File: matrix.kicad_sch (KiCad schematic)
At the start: 129 parts

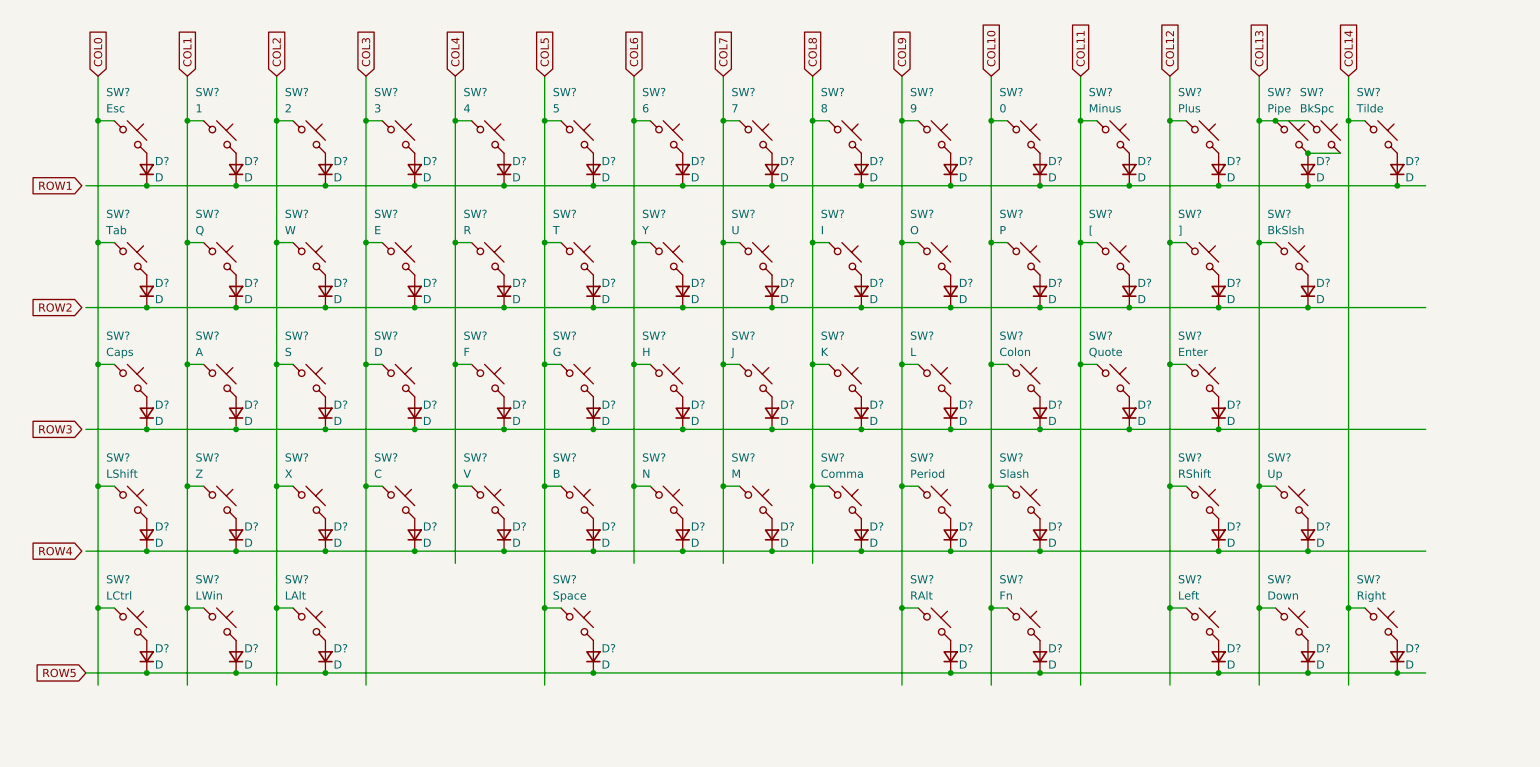
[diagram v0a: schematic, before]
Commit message: did initial routing of MCU and USB
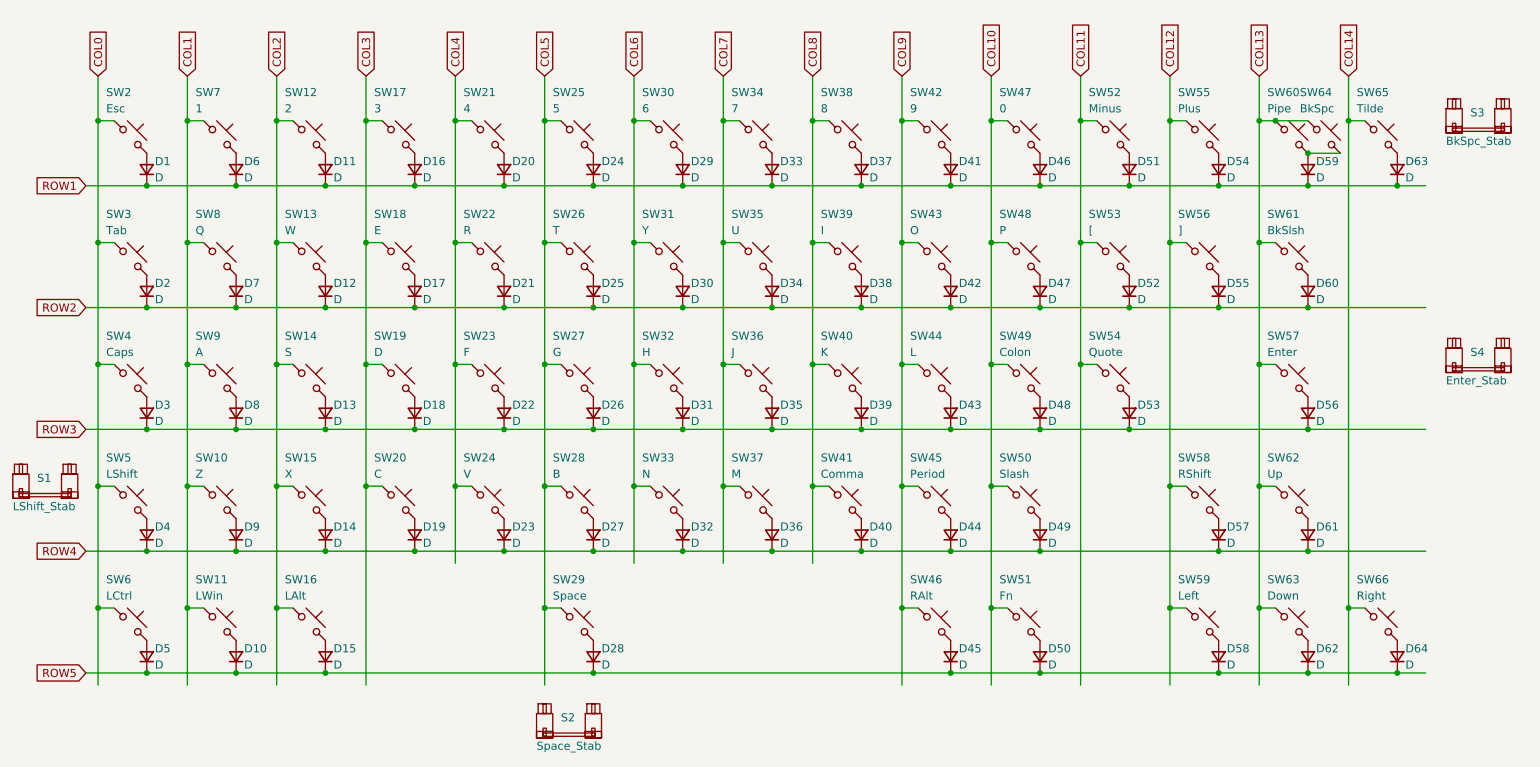
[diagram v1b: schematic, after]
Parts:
- added S1: LShift_Stab, marbastlib-mx:STAB_MX_P_2.25u, symbol marbastlib-mx:MX_stab
- added S2: Space_Stab, marbastlib-mx:STAB_MX_P_6.25u, symbol marbastlib-mx:MX_stab
- added S3: BkSpc_Stab, marbastlib-mx:STAB_MX_P_2u, symbol marbastlib-mx:MX_stab
- added S4: Enter_Stab, marbastlib-mx:STAB_MX_P_2.25u, symbol marbastlib-mx:MX_stab
- D1, D10, D11, D12, D13, D14, D15, D16, D17, D18, D19, D2, D20, D21, D22, D23, D24, D25, D26, D27, D28, D29, D3, D30, D31, D32, D33, D34, D35, D36, D37, D38, D39, D4, D40, D41, D42, D43, D44, D45, D46, D47, D48, D49, D5, D50, D51, D52, D53, D54, D55, D56, D57, D58, D59, D6, D60, D61, D62, D63, D64, D7, D8, D9: renamed from D?; footprint (none) -> Diode_SMD:D_0805_2012Metric_Pad1.15x1.40mm_HandSolder
- SW11, SW16, SW46, SW51, SW6: renamed from SW?; footprint marbastlib-mx:SW_MX_HS_1u -> marbastlib-mx:SW_MX_HS_1.25u
- SW3, SW61: renamed from SW?; footprint marbastlib-mx:SW_MX_HS_1u -> marbastlib-mx:SW_MX_HS_1.5u
- SW4, SW58: renamed from SW?; footprint marbastlib-mx:SW_MX_HS_1u -> marbastlib-mx:SW_MX_HS_1.75u
- gave numbers to parts that had none: 56
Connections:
- net COL12: no longer SW57.1
- net COL13: now also SW57.1
- net ROW1: now also D1.1 (K), D11.1 (K), D16.1 (K), D20.1 (K), D24.1 (K), D29.1 (K), D33.1 (K), D37.1 (K), D41.1 (K), D46.1 (K), D51.1 (K), D54.1 (K), D59.1 (K), D6.1 (K), D63.1 (K)
- net ROW2: now also D12.1 (K), D17.1 (K), D2.1 (K), D21.1 (K), D25.1 (K), D30.1 (K), D34.1 (K), D38.1 (K), D42.1 (K), D47.1 (K), D52.1 (K), D55.1 (K), D60.1 (K), D7.1 (K)
- net ROW3: now also D13.1 (K), D18.1 (K), D22.1 (K), D26.1 (K), D3.1 (K), D31.1 (K), D35.1 (K), D39.1 (K), D43.1 (K), D48.1 (K), D53.1 (K), D56.1 (K), D8.1 (K)
- net ROW4: now also D14.1 (K), D19.1 (K), D23.1 (K), D27.1 (K), D32.1 (K), D36.1 (K), D4.1 (K), D40.1 (K), D44.1 (K), D49.1 (K), D57.1 (K), D61.1 (K), D9.1 (K)
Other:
- moved on the sheet: D56, SW57

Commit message: routed columns
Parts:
- renumbered D57 to D56, D58 to D57, D59 to D58, D60 to D59, D56 to D60, SW9 to SW10, SW10 to SW11, SW11 to SW12, SW12 to SW13, SW13 to SW14, SW14 to SW15, SW15 to SW16, SW16 to SW17, SW17 to SW18, SW18 to SW19, SW19 to SW20, SW20 to SW21, SW21 to SW22, SW22 to SW23, SW23 to SW24, SW24 to SW25, SW25 to SW26, SW26 to SW27, SW27 to SW28, SW28 to SW29, SW2 to SW3, SW29 to SW30, SW30 to SW31, SW31 to SW32, SW32 to SW33, SW33 to SW34, SW34 to SW35, SW35 to SW36, SW36 to SW37, SW37 to SW38, SW38 to SW39, SW3 to SW4, SW39 to SW40, SW40 to SW41, SW41 to SW42, SW42 to SW43, SW43 to SW44, SW44 to SW45, SW45 to SW46, SW46 to SW47, SW47 to SW48, SW48 to SW49, SW4 to SW5, SW49 to SW50, SW50 to SW51, SW51 to SW52, SW52 to SW53, SW53 to SW54, SW54 to SW55, SW55 to SW56, SW56 to SW57, SW5 to SW6, SW57 to SW62, SW62 to SW63, SW63 to SW64, SW64 to SW65, SW65 to SW66, SW66 to SW67, SW6 to SW7, SW7 to SW8, SW8 to SW9
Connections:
- net ROW5 is gone; now on net ROW4: D10.1 (K), D15.1 (K), D28.1 (K), D45.1 (K), D5.1 (K), D50.1 (K), D57.1 (K), D62.1 (K), D64.1 (K)
- net ROW1: now also D12.1 (K), D17.1 (K), D2.1 (K), D21.1 (K), D25.1 (K), D30.1 (K), D34.1 (K), D38.1 (K), D42.1 (K), D47.1 (K), D52.1 (K), D55.1 (K), D59.1 (K), D7.1 (K); no longer D1.1 (K), D11.1 (K), D16.1 (K), D20.1 (K), D24.1 (K), D29.1 (K), D33.1 (K), D37.1 (K), D41.1 (K), D46.1 (K), D51.1 (K), D54.1 (K), D58.1 (K), D6.1 (K), D63.1 (K)
- net ROW2: now also D13.1 (K), D18.1 (K), D22.1 (K), D26.1 (K), D3.1 (K), D31.1 (K), D35.1 (K), D39.1 (K), D43.1 (K), D48.1 (K), D53.1 (K), D60.1 (K), D8.1 (K); no longer D12.1 (K), D17.1 (K), D2.1 (K), D21.1 (K), D25.1 (K), D30.1 (K), D34.1 (K), D38.1 (K), D42.1 (K), D47.1 (K), D52.1 (K), D55.1 (K), D59.1 (K), D7.1 (K)
- net ROW3: now also D14.1 (K), D19.1 (K), D23.1 (K), D27.1 (K), D32.1 (K), D36.1 (K), D4.1 (K), D40.1 (K), D44.1 (K), D49.1 (K), D56.1 (K), D61.1 (K), D9.1 (K); no longer D13.1 (K), D18.1 (K), D22.1 (K), D26.1 (K), D3.1 (K), D31.1 (K), D35.1 (K), D39.1 (K), D43.1 (K), D48.1 (K), D53.1 (K), D60.1 (K), D8.1 (K)
- net ROW4: no longer D14.1 (K), D19.1 (K), D23.1 (K), D27.1 (K), D32.1 (K), D36.1 (K), D4.1 (K), D40.1 (K), D44.1 (K), D49.1 (K), D56.1 (K), D61.1 (K), D9.1 (K)
- new net ROW0: D1.1 (K), D11.1 (K), D16.1 (K), D20.1 (K), D24.1 (K), D29.1 (K), D33.1 (K), D37.1 (K), D41.1 (K), D46.1 (K), D51.1 (K), D54.1 (K), D58.1 (K), D6.1 (K), D63.1 (K)

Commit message: completed route pass 1
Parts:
- SW60, SW65, SW66: footprint marbastlib-mx:SW_MX_HS_1u -> marbastlib-mx:SW_MX_HS_S_1u
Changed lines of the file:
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@@
       (effects (font (size 1.27 1.27)) (justify left))
     )
-    (property "Footprint" "marbastlib-mx:SW_MX_HS_1u" (id 2) (at 233.045 57.785 0)
+    (property "Footprint" "marbastlib-mx:SW_MX_HS_S_1u" (id 2) (at 233.045 57.785 0)
       (effects (font (size 1.27 1.27)) hide)
     )
@@
       (effects (font (size 1.27 1.27)) (justify left))
     )
-    (property "Footprint" "marbastlib-mx:SW_MX_HS_1u" (id 2) (at 238.125 57.785 0)
+    (property "Footprint" "marbastlib-mx:SW_MX_HS_S_1u" (id 2) (at 238.125 57.785 0)
       (effects (font (size 1.27 1.27)) hide)
     )
@@
       (effects (font (size 1.27 1.27)) (justify left))
     )
-    (property "Footprint" "marbastlib-mx:SW_MX_HS_1u" (id 2) (at 247.015 57.785 0)
-      (effects (font (size 1.27 1.27)) hide)
-    )
+    (property "Footprint" "marbastlib-mx:SW_MX_HS_S_1u" (id 2) (at 247.015 57.785 0)
+      (effects (font (size 1.27 1.27)) hide)
+    )
